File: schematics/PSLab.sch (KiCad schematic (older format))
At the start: 74 parts, among them CON1 USB-MINI-B, J1 Programmer, J10 GND, J11 Vbus, J13 D+, J14 D-, J16 I2C-2, J2 DoublePins, J3 LA, J5 Bluetooth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

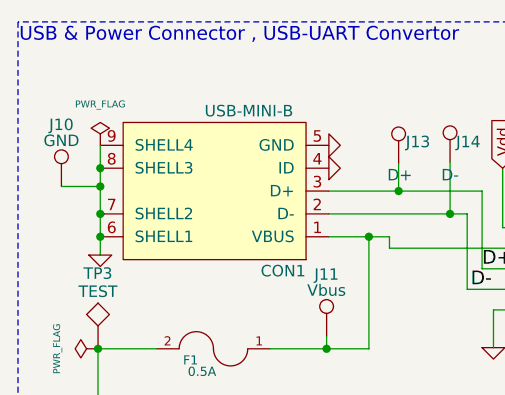
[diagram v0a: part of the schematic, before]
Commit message: feat: added components for RTC
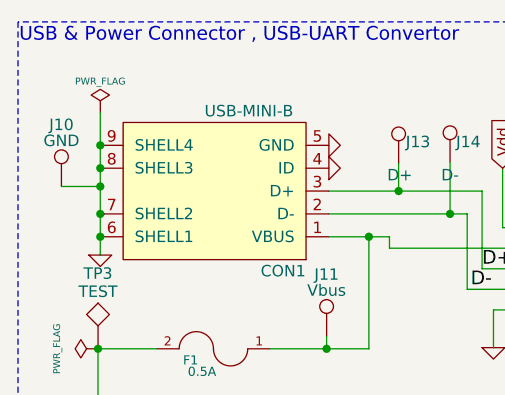
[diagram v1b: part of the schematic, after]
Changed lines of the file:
@@
 L power:PWR_FLAG #FLG010
 U 1 1 54C819ED
-P 860 1040
-F 0 "#FLG010" H 860 1135 30  0001 C CNN
-F 1 "PWR_FLAG" H 860 1220 30  0000 C CNN
-F 2 "" H 860 1040 60  0000 C CNN
-F 3 "" H 860 1040 60  0000 C CNN
-	1    860  1040
+P 860 895
+F 0 "#FLG010" H 860 990 30  0001 C CNN
+F 1 "PWR_FLAG" H 860 1030 30  0000 C CNN
+F 2 "" H 860 895 60  0000 C CNN
+F 3 "" H 860 895 60  0000 C CNN
+	1    860  895
 	1    0    0    -1
 $EndComp
@@
 	4605 815  4545 815
 Wire Wire Line
-	860  1040 860  1140
+	860  895  860  1040
 Connection ~ 860  1440
 Connection ~ 860  1340
@@
 Wire Wire Line
 	8900 1025 8700 1025
+Connection ~ 860  1040
+Wire Wire Line
+	860  1040 860  1140
 $EndSCHEMATC

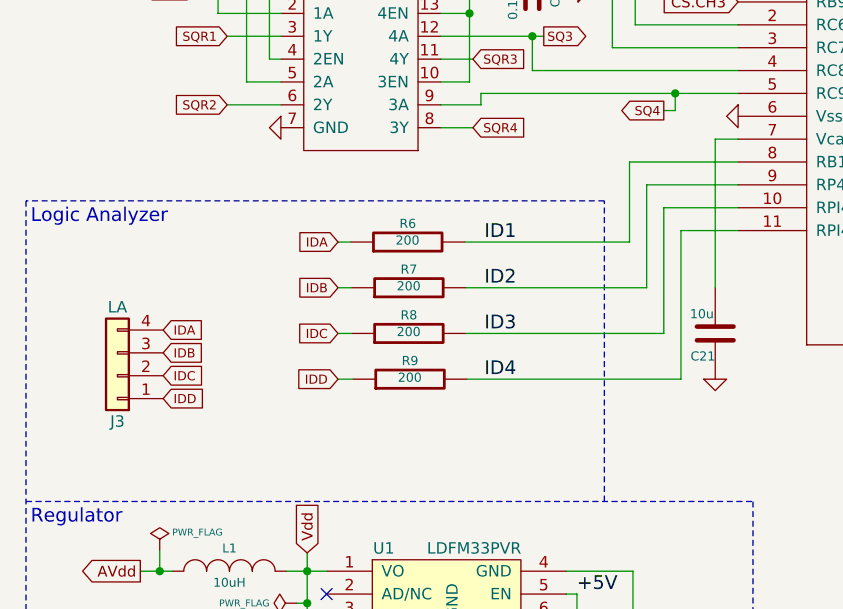
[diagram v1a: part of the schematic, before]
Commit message: route: adding missing routes after importing net
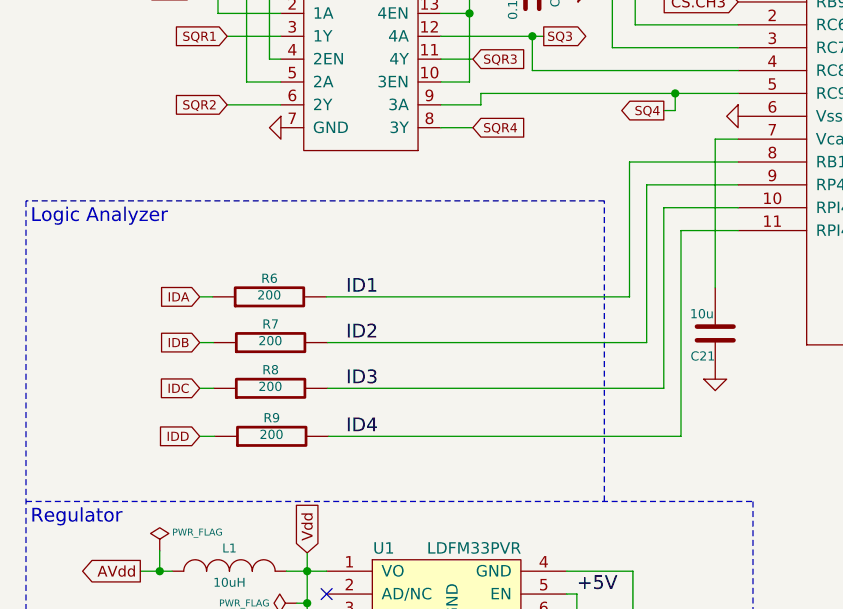
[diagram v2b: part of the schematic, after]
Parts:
- removed J3: LA, Pin_Headers:Pin_Header_Straight_1x04_Pitch2.54mm, symbol PSLab-rescue:Conn_01x04
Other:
- moved on the sheet: R6, R7, R8, R9
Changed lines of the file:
@@
 L PSLab-rescue:R-RESCUE-proto1 R7
 U 1 1 542393BE
-P 2210 4650
-F 0 "R7" V 2290 4650 40  0000 C CNN
-F 1 "200" V 2217 4651 40  0000 C CNN
-F 2 "Resistors_SMD:R_0603" V 2140 4650 30  0001 C CNN
-F 3 "" H 2210 4650 30  0000 C CNN
-	1    2210 4650
+P 1605 4890
+F 0 "R7" V 1685 4890 40  0000 C CNN
+F 1 "200" V 1612 4891 40  0000 C CNN
+F 2 "Resistors_SMD:R_0603" V 1535 4890 30  0001 C CNN
+F 3 "" H 1605 4890 30  0000 C CNN
+	1    1605 4890
 	0    -1   -1   0
 $EndComp
@@
 L PSLab-rescue:R-RESCUE-proto1 R6
 U 1 1 54239455
-P 2205 4450
-F 0 "R6" V 2285 4450 40  0000 C CNN
-F 1 "200" V 2212 4451 40  0000 C CNN
-F 2 "Resistors_SMD:R_0603" V 2135 4450 30  0001 C CNN
-F 3 "" H 2205 4450 30  0000 C CNN
-	1    2205 4450
+P 1600 4690
+F 0 "R6" V 1680 4690 40  0000 C CNN
+F 1 "200" V 1607 4691 40  0000 C CNN
+F 2 "Resistors_SMD:R_0603" V 1530 4690 30  0001 C CNN
+F 3 "" H 1600 4690 30  0000 C CNN
+	1    1600 4690
 	0    -1   -1   0
 $EndComp
@@
 L PSLab-rescue:R-RESCUE-proto1 R8
 U 1 1 555DB0AF
-P 2210 4850
-F 0 "R8" V 2290 4850 40  0000 C CNN
-F 1 "200" V 2217 4851 40  0000 C CNN
-F 2 "Resistors_SMD:R_0603" V 2140 4850 30  0001 C CNN
-F 3 "" H 2210 4850 30  0000 C CNN
-	1    2210 4850
+P 1605 5090
+F 0 "R8" V 1685 5090 40  0000 C CNN
+F 1 "200" V 1612 5091 40  0000 C CNN
+F 2 "Resistors_SMD:R_0603" V 1535 5090 30  0001 C CNN
+F 3 "" H 1605 5090 30  0000 C CNN
+	1    1605 5090
 	0    -1   -1   0
 $EndComp
@@
 L PSLab-rescue:R-RESCUE-proto1 R9
 U 1 1 555DB131
-P 2215 5050
-F 0 "R9" V 2295 5050 40  0000 C CNN
-F 1 "200" V 2222 5051 40  0000 C CNN
-F 2 "Resistors_SMD:R_0603" V 2145 5050 30  0001 C CNN
-F 3 "" H 2215 5050 30  0000 C CNN
-	1    2215 5050
+P 1610 5300
+F 0 "R9" V 1690 5300 40  0000 C CNN
+F 1 "200" V 1617 5301 40  0000 C CNN
+F 2 "Resistors_SMD:R_0603" V 1540 5300 30  0001 C CNN
+F 3 "" H 1610 5300 30  0000 C CNN
+	1    1610 5300
 	0    -1   -1   0
 $EndComp
@@
 Text Label 7300 2750 0    60   ~ 0
 Vdd
-Text Label 2540 4450 0    60   ~ 0
+Text Label 1935 4690 0    60   ~ 0
 ID1
-Text Label 2540 4650 0    60   ~ 0
+Text Label 1935 4890 0    60   ~ 0
 ID2
-Text Label 2540 4850 0    60   ~ 0
+Text Label 1935 5090 0    60   ~ 0
 ID3
-Text Label 2540 5050 0    60   ~ 0
+Text Label 1935 5300 0    60   ~ 0
 ID4
 Text GLabel 8025 2700 0    60   Input ~ 0
@@
 Text GLabel 6775 1895 1    40   Input ~ 0
 +5V
-$Comp
-L PSLab-rescue:Conn_01x04 J3
-U 1 1 5AD4C0DD
-P 935 5035
-F 0 "J3" H 935 5235 50  0000 C CNN
-F 1 "LA" H 935 4735 50  0000 C CNN
-F 2 "Pin_Headers:Pin_Header_Straight_1x04_Pitch2.54mm" H 935 5035 50  0001 C CNN
-F 3 "" H 935 5035 50  0001 C CNN
-	1    935  5035
-	-1   0    0    1
-$EndComp
 Text GLabel 1415 3550 0    40   Input ~ 0
 SQR1
@@
 Text GLabel 2490 3950 2    40   Input ~ 0
 SQR4
-Text GLabel 1900 5050 0    40   Input ~ 0
+Text GLabel 1295 5300 0    40   Input ~ 0
 IDD
-Text GLabel 1900 4850 0    40   Input ~ 0
+Text GLabel 1295 5090 0    40   Input ~ 0
 IDC
-Text GLabel 1900 4650 0    40   Input ~ 0
+Text GLabel 1295 4890 0    40   Input ~ 0
 IDB
-Text GLabel 1900 4450 0    40   Input ~ 0
+Text GLabel 1295 4690 0    40   Input ~ 0
 IDA
-Text GLabel 1135 4835 2    40   Input ~ 0
-IDA
-Text GLabel 1135 4935 2    40   Input ~ 0
-IDB
-Text GLabel 1135 5035 2    40   Input ~ 0
-IDC
-Text GLabel 1135 5135 2    40   Input ~ 0
-IDD
 Text GLabel 6085 7165 0    40   Input ~ 0
 IDD
@@
 	3650 3500 3200 3500
 Wire Wire Line
-	3250 4200 3250 4650
-Wire Wire Line
-	3325 4300 3325 4850
-Wire Wire Line
-	3400 4400 3400 5050
-Wire Wire Line
 	1375 3450 1375 3025
 Wire Wire Line
@@
 Wire Wire Line
 	2350 3550 2750 3550
-Wire Wire Line
-	3175 4100 3175 4450
 Wire Wire Line
 	2525 3800 3375 3800
@@
 	535  5585 3715 5585
 Wire Wire Line
-	3175 4450 2455 4450
-Wire Wire Line
-	3250 4650 2460 4650
-Wire Wire Line
-	3325 4850 2460 4850
-Wire Wire Line
-	3400 5050 2465 5050
-Wire Wire Line
 	6975 850  6975 1495
 Connection ~ 6975 850
@@
 	2750 3700 3650 3700
 Wire Wire Line
-	1955 4450 1900 4450
-Wire Wire Line
-	1960 4650 1900 4650
-Wire Wire Line
-	1965 5050 1900 5050
-Wire Wire Line
-	1960 4850 1900 4850
+	1350 4690 1295 4690
+Wire Wire Line
+	1355 4890 1295 4890
+Wire Wire Line
+	1360 5300 1295 5300
+Wire Wire Line
+	1355 5090 1295 5090
 Wire Wire Line
 	6570 4525 6525 4525
@@
 Wire Wire Line
 	860  1040 860  1140
+Wire Wire Line
+	3400 4400 3400 5300
+Wire Wire Line
+	1860 5300 3400 5300
+Wire Wire Line
+	3325 4300 3325 5090
+Wire Wire Line
+	1855 5090 3325 5090
+Wire Wire Line
+	3250 4200 3250 4890
+Wire Wire Line
+	1855 4890 3250 4890
+Wire Wire Line
+	3175 4100 3175 4690
+Wire Wire Line
+	1850 4690 3175 4690
 $EndSCHEMATC
